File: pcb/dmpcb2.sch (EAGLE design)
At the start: 65 parts, among them IC1 7805DT, IC2 L293D, IC4 LM358D, IC5 LM358D, J7 SJ-3523-SMT-TR, Q1 IRF530, Q2 IRF530

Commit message: borading2..
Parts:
- added DCMOTOR1: (no value), SparkFun-Connectors:CONN_022.54MM_SCREWTERM
- added JP1: (no value), jumper:JP2E
- added X2: (no value), con-wago-500:W237-4
- added X3: (no value), con-wago-500:W237-102
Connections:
- new net N$11: DCMOTOR1.1, IC2.4Y
- new net N$12: DCMOTOR1.2, IC2.3Y
- net +5V: now also JP1.3
- net A1: now also X2-2.KL
- net A2: now also X2-1.KL
- net B1: now also X2-3.KL
- net B2: now also X2-4.KL
- net GND: now also X3-2.KL
- net V+: now also JP1.1
- net VMOT: now also JP1.2, X3-1.KL
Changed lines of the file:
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@@
 <part name="D3" library="diode" library_urn="urn:adsk.eagle:library:210" deviceset="1N4148" device="DO35-7" package3d_urn="urn:adsk.eagle:package:43339/2"/>
 <part name="D4" library="diode" library_urn="urn:adsk.eagle:library:210" deviceset="1N4148" device="DO35-7" package3d_urn="urn:adsk.eagle:package:43339/2"/>
+<part name="X2" library="con-wago-500" library_urn="urn:adsk.eagle:library:195" deviceset="W237-4" device="" package3d_urn="urn:adsk.eagle:package:10695/1"/>
+<part name="X3" library="con-wago-500" library_urn="urn:adsk.eagle:library:195" deviceset="W237-102" device="" package3d_urn="urn:adsk.eagle:package:10688/1"/>
+<part name="GND25" library="supply1" library_urn="urn:adsk.eagle:library:371" deviceset="GND" device=""/>
+<part name="JP1" library="jumper" library_urn="urn:adsk.eagle:library:252" deviceset="JP2E" device="" package3d_urn="urn:adsk.eagle:package:15452/1"/>
+<part name="SUPPLY16" library="supply2" library_urn="urn:adsk.eagle:library:372" deviceset="+5V" device=""/>
+<part name="DCMOTOR1" library="SparkFun-Connectors" library_urn="urn:adsk.eagle:library:513" deviceset="CONN_02" device="2.54MM_SCREWTERM" package3d_urn="urn:adsk.eagle:package:38059/1"/>
 </parts>
 <sheets>
@@
 <attribute name="VALUE" x="261.62" y="116.6114" size="1.778" layer="96" rot="R180"/>
 </instance>
+<instance part="X2" gate="-1" x="414.02" y="91.44" smashed="yes" rot="R180">
+<attribute name="NAME" x="414.02" y="90.551" size="1.778" layer="95"/>
+</instance>
+<instance part="X2" gate="-2" x="414.02" y="96.52" smashed="yes" rot="R180">
+<attribute name="NAME" x="414.02" y="95.631" size="1.778" layer="95"/>
+</instance>
+<instance part="X2" gate="-3" x="414.02" y="101.6" smashed="yes" rot="R180">
+<attribute name="NAME" x="414.02" y="100.711" size="1.778" layer="95"/>
+</instance>
+<instance part="X2" gate="-4" x="414.02" y="106.68" smashed="yes" rot="R180">
+<attribute name="VALUE" x="416.56" y="110.363" size="1.778" layer="96" rot="R180"/>
+<attribute name="NAME" x="414.02" y="105.791" size="1.778" layer="95"/>
+</instance>
+<instance part="X3" gate="-1" x="414.02" y="114.3" smashed="yes" rot="R180">
+<attribute name="NAME" x="414.02" y="113.411" size="1.778" layer="95"/>
+</instance>
+<instance part="X3" gate="-2" x="414.02" y="121.92" smashed="yes" rot="R180">
+<attribute name="VALUE" x="416.56" y="125.603" size="1.778" layer="96" rot="R180"/>
+<attribute name="NAME" x="414.02" y="121.031" size="1.778" layer="95"/>
+</instance>
+<instance part="GND25" gate="1" x="393.7" y="121.92" smashed="yes" rot="R270">
+<attribute name="VALUE" x="391.16" y="124.46" size="1.778" layer="96" rot="R270"/>
+</instance>
+<instance part="JP1" gate="1" x="406.4" y="137.16" smashed="yes">
+<attribute name="NAME" x="402.59" y="137.16" size="1.778" layer="95" rot="R90"/>
+<attribute name="VALUE" x="412.115" y="137.16" size="1.778" layer="96" rot="R90"/>
+</instance>
+<instance part="SUPPLY16" gate="+5V" x="416.56" y="132.08" smashed="yes" rot="R270">
+<attribute name="VALUE" x="419.735" y="132.715" size="1.778" layer="96"/>
+</instance>
+<instance part="DCMOTOR1" gate="G$1" x="411.48" y="187.96" smashed="yes" rot="R180">
+<attribute name="VALUE" x="414.02" y="192.786" size="1.778" layer="96" font="vector" rot="R180"/>
+<attribute name="NAME" x="414.02" y="182.372" size="1.778" layer="95" font="vector" rot="R180"/>
+</instance>
 </instances>
 <busses>
@@
 <junction x="297.18" y="114.3"/>
 </segment>
+<segment>
+<pinref part="X3" gate="-2" pin="KL"/>
+<wire x1="408.94" y1="121.92" x2="396.24" y2="121.92" width="0.1524" layer="91"/>
+<pinref part="GND25" gate="1" pin="GND"/>
+</segment>
 </net>
 <net name="V+" class="0">
@@
 <wire x1="345.44" y1="154.94" x2="345.44" y2="162.56" width="0.1524" layer="91"/>
 <wire x1="345.44" y1="162.56" x2="347.98" y2="162.56" width="0.1524" layer="91"/>
+</segment>
+<segment>
+<pinref part="JP1" gate="1" pin="1"/>
+<wire x1="403.86" y1="134.62" x2="403.86" y2="127" width="0.1524" layer="91"/>
+<wire x1="403.86" y1="127" x2="414.02" y2="127" width="0.1524" layer="91"/>
+<label x="414.02" y="127" size="1.778" layer="95"/>
 </segment>
 </net>
@@
 <wire x1="114.3" y1="129.54" x2="114.3" y2="121.92" width="0.1524" layer="91"/>
 </segment>
+<segment>
+<pinref part="JP1" gate="1" pin="3"/>
+<wire x1="408.94" y1="134.62" x2="408.94" y2="132.08" width="0.1524" layer="91"/>
+<wire x1="408.94" y1="132.08" x2="414.02" y2="132.08" width="0.1524" layer="91"/>
+<pinref part="SUPPLY16" gate="+5V" pin="+5V"/>
+</segment>
 </net>
 <net name="N$2" class="0">
@@
 <net name="B2" class="0">
 <segment>
-<wire x1="373.38" y1="101.6" x2="375.92" y2="101.6" width="0.1524" layer="91"/>
 <label x="375.92" y="101.6" size="1.778" layer="95" xref="yes"/>
 <pinref part="U$2" gate="G$1" pin="B2"/>
+<pinref part="X2" gate="-4" pin="KL"/>
+<wire x1="408.94" y1="106.68" x2="396.24" y2="106.68" width="0.1524" layer="91"/>
+<wire x1="396.24" y1="106.68" x2="396.24" y2="101.6" width="0.1524" layer="91"/>
+<wire x1="396.24" y1="101.6" x2="373.38" y2="101.6" width="0.1524" layer="91"/>
 </segment>
 </net>
@@
 <segment>
 <label x="386.08" y="99.06" size="1.778" layer="95" xref="yes"/>
-<wire x1="373.38" y1="99.06" x2="386.08" y2="99.06" width="0.1524" layer="91"/>
 <pinref part="U$2" gate="G$1" pin="B1"/>
+<wire x1="373.38" y1="99.06" x2="403.86" y2="99.06" width="0.1524" layer="91"/>
+<wire x1="403.86" y1="99.06" x2="403.86" y2="101.6" width="0.1524" layer="91"/>
+<pinref part="X2" gate="-3" pin="KL"/>
+<wire x1="403.86" y1="101.6" x2="408.94" y2="101.6" width="0.1524" layer="91"/>
 </segment>
 </net>
 <net name="A1" class="0">
 <segment>
-<wire x1="373.38" y1="96.52" x2="375.92" y2="96.52" width="0.1524" layer="91"/>
 <label x="375.92" y="96.52" size="1.778" layer="95" xref="yes"/>
 <pinref part="U$2" gate="G$1" pin="A1"/>
+<pinref part="X2" gate="-2" pin="KL"/>
+<wire x1="373.38" y1="96.52" x2="408.94" y2="96.52" width="0.1524" layer="91"/>
 </segment>
 </net>
@@
 <segment>
 <label x="386.08" y="93.98" size="1.778" layer="95" xref="yes"/>
-<wire x1="373.38" y1="93.98" x2="386.08" y2="93.98" width="0.1524" layer="91"/>
+<wire x1="373.38" y1="93.98" x2="393.7" y2="93.98" width="0.1524" layer="91"/>
 <pinref part="U$2" gate="G$1" pin="A2"/>
+<wire x1="393.7" y1="93.98" x2="393.7" y2="91.44" width="0.1524" layer="91"/>
+<pinref part="X2" gate="-1" pin="KL"/>
+<wire x1="393.7" y1="91.44" x2="408.94" y2="91.44" width="0.1524" layer="91"/>
 </segment>
 </net>
@@
 <wire x1="373.38" y1="114.3" x2="381" y2="114.3" width="0.1524" layer="91"/>
 <pinref part="C7" gate="G$1" pin="+"/>
-<wire x1="381" y1="114.3" x2="386.08" y2="114.3" width="0.1524" layer="91"/>
 <label x="386.08" y="114.3" size="1.778" layer="95" xref="yes"/>
+<wire x1="381" y1="114.3" x2="406.4" y2="114.3" width="0.1524" layer="91"/>
+<pinref part="X3" gate="-1" pin="KL"/>
+<wire x1="406.4" y1="114.3" x2="408.94" y2="114.3" width="0.1524" layer="91"/>
+<wire x1="406.4" y1="114.3" x2="406.4" y2="134.62" width="0.1524" layer="91"/>
+<junction x="406.4" y="114.3"/>
+<pinref part="JP1" gate="1" pin="2"/>
 </segment>
 </net>
@@
 </segment>
 </net>
+<net name="N$11" class="0">
+<segment>
+<pinref part="IC2" gate="G$1" pin="4Y"/>
+<pinref part="DCMOTOR1" gate="G$1" pin="1"/>
+<wire x1="378.46" y1="187.96" x2="403.86" y2="187.96" width="0.1524" layer="91"/>
+</segment>
+</net>
+<net name="N$12" class="0">
+<segment>
+<pinref part="DCMOTOR1" gate="G$1" pin="2"/>
+<wire x1="403.86" y1="185.42" x2="391.16" y2="185.42" width="0.1524" layer="91"/>
+<wire x1="391.16" y1="185.42" x2="391.16" y2="172.72" width="0.1524" layer="91"/>
+<pinref part="IC2" gate="G$1" pin="3Y"/>
+<wire x1="391.16" y1="172.72" x2="378.46" y2="172.72" width="0.1524" layer="91"/>
+</segment>
+</net>

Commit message: routing done
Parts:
- removed DCMOTOR, DCMOTOR1, SENSOR, SWITCHLOAD, SWITCHLOAD1: (no value), SparkFun-Connectors:CONN_022.54MM_SCREWTERM
- removed SV2: (no value), con-lstb:MA08-1
- added J3: (no value), SparkFun-Connectors:CONN_08"
- added J4: (no value), SparkFun-Connectors:CONN_03LOCK_LONGPADS
- added X4, X5, X6, X7, X8: (no value), con-wago-500:W237-102
- renumbered JP7 to EXT_5V, JP8 to 14/DAC
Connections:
- removed net LM293EN: IC2.1-2EN, SV2.3
- removed net LM293IN01: IC2.1A, SV2.4
- removed net LM293IN02: IC2.2A, SV2.5
- new net H-BRDIGE_A_02: IC2.2A, J3.5
- new net H-BRIDGE_A_01: IC2.1A, J3.4
- new net H-BRIDGE_A_EN: IC2.1-2EN, J3.3
- new net H-BRIDGE_B_01: IC2.4A, J4.3
- new net H-BRIDGE_B_02: IC2.3A, J4.2
- new net H-BRIDGE_B_EN: IC2.3-4EN, J4.1
- net +5V: now also X8-1.KL; no longer SENSOR.2
- net BUTTON01: now also J3.1; no longer SV2.1
- net BUTTON02: now also J3.2; no longer SV2.2
- net DRV8825DIR: now also J1.1; no longer J1.2
- net DRV8825EN: now also J1.5; no longer J1.1
- net DRV8825SLP: now also J1.3; no longer J1.5
- net DRV8825STEP: now also J1.2; no longer J1.3
- net M1: now also X4-2.KL; no longer SWITCHLOAD.1
- net M2: now also X5-2.KL; no longer SWITCHLOAD1.1
- net MAX7219CLK: now also J3.7; no longer SV2.7
- net MAX7219CS: now also J3.8; no longer SV2.8
- net MAX7219DIN: now also J3.6; no longer SV2.6
- net N$11: now also X6-2.KL; no longer DCMOTOR1.1
- net N$12: now also X6-1.KL; no longer DCMOTOR1.2
- net N$5: now also X7-1.KL; no longer DCMOTOR.2
- net N$6: now also X7-2.KL; no longer DCMOTOR.1
- net SENSORPORT: now also X8-2.KL; no longer SENSOR.1
- net V+: now also X4-1.KL, X5-1.KL; no longer SWITCHLOAD.2, SWITCHLOAD1.2
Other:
- moved on the sheet: JP3

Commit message: started to add part references and values, also started adding pin names and similar. tried adding nice graphics as bmp but failed horribly...
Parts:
- R4: value 220 -> 220R
- renumbered JP6 to STP_CONF, LED1 to LED_01, U$1 to TEENSY3.2, U$2 to DRV8825

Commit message: issues added and fixed
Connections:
- removed net N$19: S1.S, S1.S1
- removed net N$21: S2.S, S2.S1
- net 3.3V: now also S1.S, S1.S1, S2.S, S2.S1
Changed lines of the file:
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@@
 <?xml version="1.0" encoding="utf-8"?>
 <!DOCTYPE eagle SYSTEM "eagle.dtd">
-<eagle version="9.4.2">
+<eagle version="9.5.2">
 <drawing>
 <settings>
@@
 <wire x1="187.96" y1="157.48" x2="187.96" y2="152.4" width="0.1524" layer="91"/>
 <label x="187.96" y="152.4" size="1.778" layer="95" rot="R270" xref="yes"/>
-<label x="261.62" y="43.18" size="1.778" layer="95" rot="R90" xref="yes"/>
-</segment>
-<segment>
-<label x="289.56" y="43.18" size="1.778" layer="95" rot="R90" xref="yes"/>
 </segment>
 <segment>
@@
 <wire x1="83.82" y1="124.46" x2="83.82" y2="116.84" width="0.1524" layer="91"/>
 </segment>
+<segment>
+<pinref part="S1" gate="1" pin="S"/>
+<wire x1="261.62" y1="43.18" x2="261.62" y2="40.64" width="0.1524" layer="91"/>
+<pinref part="S1" gate="1" pin="S1"/>
+<wire x1="261.62" y1="40.64" x2="264.16" y2="40.64" width="0.1524" layer="91"/>
+<junction x="264.16" y="40.64"/>
+<junction x="261.62" y="40.64"/>
+<pinref part="S2" gate="1" pin="S"/>
+<wire x1="289.56" y1="43.18" x2="289.56" y2="40.64" width="0.1524" layer="91"/>
+<pinref part="S2" gate="1" pin="S1"/>
+<wire x1="289.56" y1="40.64" x2="292.1" y2="40.64" width="0.1524" layer="91"/>
+<junction x="289.56" y="40.64"/>
+<junction x="292.1" y="40.64"/>
+<wire x1="261.62" y1="43.18" x2="289.56" y2="43.18" width="0.1524" layer="91"/>
+<label x="274.32" y="43.18" size="1.778" layer="95" rot="R90" xref="yes"/>
+</segment>
 </net>
 <net name="N$14" class="0">
@@
 </segment>
 </net>
-<net name="N$19" class="0">
-<segment>
-<pinref part="S1" gate="1" pin="S"/>
-<wire x1="261.62" y1="43.18" x2="261.62" y2="40.64" width="0.1524" layer="91"/>
-<pinref part="S1" gate="1" pin="S1"/>
-<wire x1="261.62" y1="40.64" x2="264.16" y2="40.64" width="0.1524" layer="91"/>
-<junction x="264.16" y="40.64"/>
-<junction x="261.62" y="40.64"/>
-</segment>
-</net>
-<net name="N$21" class="0">
-<segment>
-<pinref part="S2" gate="1" pin="S"/>
-<wire x1="289.56" y1="43.18" x2="289.56" y2="40.64" width="0.1524" layer="91"/>
-<pinref part="S2" gate="1" pin="S1"/>
-<wire x1="289.56" y1="40.64" x2="292.1" y2="40.64" width="0.1524" layer="91"/>
-<junction x="289.56" y="40.64"/>
-<junction x="292.1" y="40.64"/>
-</segment>
-</net>

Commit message: added possibilty to jump out the lm7805
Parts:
- added EXT_5V1: (no value), jumper:JP1E
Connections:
- new net N$19: EXT_5V1.2, IC1.VI
- net +5V: now also LED_01.A
- net N$25: no longer LED_01.A
- net V+: now also EXT_5V1.1; no longer IC1.VI
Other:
- moved on the sheet: LED_01, R4
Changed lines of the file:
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@@
 <part name="J3" library="SparkFun-Connectors" deviceset="CONN_08" device="&quot;"/>
 <part name="J4" library="SparkFun-Connectors" library_urn="urn:adsk.eagle:library:513" deviceset="CONN_03" device="LOCK_LONGPADS" package3d_urn="urn:adsk.eagle:package:38065/1"/>
+<part name="EXT_5V1" library="jumper" library_urn="urn:adsk.eagle:library:252" deviceset="JP1E" device="" package3d_urn="urn:adsk.eagle:package:15455/1"/>
 </parts>
 <sheets>
@@
 <attribute name="VALUE" x="54.102" y="196.85" size="1.778" layer="96" rot="R90"/>
 </instance>
-<instance part="LED_01" gate="G$1" x="104.14" y="175.26" smashed="yes">
-<attribute name="NAME" x="107.696" y="170.688" size="1.778" layer="95" rot="R90"/>
-<attribute name="VALUE" x="109.855" y="170.688" size="1.778" layer="96" rot="R90"/>
-</instance>
-<instance part="R4" gate="G$1" x="104.14" y="162.56" smashed="yes" rot="R90">
-<attribute name="NAME" x="102.6414" y="158.75" size="1.778" layer="95" rot="R90"/>
-<attribute name="VALUE" x="107.442" y="158.75" size="1.778" layer="96" rot="R90"/>
-</instance>
-<instance part="GND9" gate="1" x="104.14" y="152.4" smashed="yes">
-<attribute name="VALUE" x="101.6" y="149.86" size="1.778" layer="96"/>
+<instance part="LED_01" gate="G$1" x="119.38" y="175.26" smashed="yes">
+<attribute name="NAME" x="122.936" y="170.688" size="1.778" layer="95" rot="R90"/>
+<attribute name="VALUE" x="125.095" y="170.688" size="1.778" layer="96" rot="R90"/>
+</instance>
+<instance part="R4" gate="G$1" x="119.38" y="165.1" smashed="yes" rot="R90">
+<attribute name="NAME" x="117.8814" y="161.29" size="1.778" layer="95" rot="R90"/>
+<attribute name="VALUE" x="122.682" y="161.29" size="1.778" layer="96" rot="R90"/>
+</instance>
+<instance part="GND9" gate="1" x="119.38" y="154.94" smashed="yes">
+<attribute name="VALUE" x="116.84" y="152.4" size="1.778" layer="96"/>
 </instance>
 <instance part="Q1" gate="G$1" x="287.02" y="111.76" smashed="yes" rot="R90">
@@
 <attribute name="VALUE" x="434.34" y="177.546" size="1.778" layer="96" font="vector" rot="R180"/>
 <attribute name="NAME" x="434.34" y="164.592" size="1.778" layer="95" font="vector" rot="R180"/>
+</instance>
+<instance part="EXT_5V1" gate="A" x="58.42" y="195.58" smashed="yes">
+<attribute name="NAME" x="57.15" y="195.58" size="1.778" layer="95" rot="R90"/>
+<attribute name="VALUE" x="64.135" y="195.58" size="1.778" layer="96" rot="R90"/>
 </instance>
 </instances>
@@
 <pinref part="R4" gate="G$1" pin="1"/>
 <pinref part="GND9" gate="1" pin="GND"/>
-<wire x1="104.14" y1="157.48" x2="104.14" y2="154.94" width="0.1524" layer="91"/>
+<wire x1="119.38" y1="160.02" x2="119.38" y2="157.48" width="0.1524" layer="91"/>
 </segment>
 <segment>
@@
 <wire x1="40.64" y1="193.04" x2="40.64" y2="182.88" width="0.1524" layer="91"/>
 <label x="48.26" y="185.42" size="1.778" layer="95"/>
-<pinref part="IC1" gate="A1" pin="VI"/>
 <wire x1="40.64" y1="182.88" x2="50.8" y2="182.88" width="0.1524" layer="91"/>
 <pinref part="C1" gate="G$1" pin="+"/>
 <wire x1="50.8" y1="182.88" x2="55.88" y2="182.88" width="0.1524" layer="91"/>
-<wire x1="55.88" y1="182.88" x2="63.5" y2="182.88" width="0.1524" layer="91"/>
 <wire x1="55.88" y1="182.88" x2="55.88" y2="177.8" width="0.1524" layer="91"/>
-<junction x="55.88" y="182.88"/>
 <pinref part="C3" gate="G$1" pin="+"/>
 <wire x1="50.8" y1="187.96" x2="50.8" y2="182.88" width="0.1524" layer="91"/>
@@
 <pinref part="X1" gate="-1" pin="KL"/>
 <junction x="40.64" y="182.88"/>
+<pinref part="EXT_5V1" gate="A" pin="1"/>
+<wire x1="55.88" y1="182.88" x2="58.42" y2="182.88" width="0.1524" layer="91"/>
+<wire x1="58.42" y1="182.88" x2="58.42" y2="193.04" width="0.1524" layer="91"/>
+<junction x="55.88" y="182.88"/>
 </segment>
 <segment>
@@
 <wire x1="114.3" y1="193.04" x2="114.3" y2="182.88" width="0.1524" layer="91"/>
 <pinref part="SUPPLY2" gate="+5V" pin="+5V"/>
-<wire x1="114.3" y1="182.88" x2="124.46" y2="182.88" width="0.1524" layer="91"/>
+<wire x1="114.3" y1="182.88" x2="119.38" y2="182.88" width="0.1524" layer="91"/>
+<pinref part="LED_01" gate="G$1" pin="A"/>
+<wire x1="119.38" y1="182.88" x2="124.46" y2="182.88" width="0.1524" layer="91"/>
+<wire x1="119.38" y1="177.8" x2="119.38" y2="182.88" width="0.1524" layer="91"/>
+<junction x="119.38" y="182.88"/>
 </segment>
 <segment>
@@
 <pinref part="LED_01" gate="G$1" pin="C"/>
 <pinref part="R4" gate="G$1" pin="2"/>
-<wire x1="104.14" y1="170.18" x2="104.14" y2="167.64" width="0.1524" layer="91"/>
 </segment>
 </net>
@@
 <pinref part="C2" gate="G$1" pin="+"/>
 <wire x1="83.82" y1="182.88" x2="88.9" y2="182.88" width="0.1524" layer="91"/>
-<wire x1="88.9" y1="182.88" x2="104.14" y2="182.88" width="0.1524" layer="91"/>
+<wire x1="88.9" y1="182.88" x2="111.76" y2="182.88" width="0.1524" layer="91"/>
 <wire x1="88.9" y1="182.88" x2="88.9" y2="177.8" width="0.1524" layer="91"/>
 <junction x="88.9" y="182.88"/>
-<pinref part="LED_01" gate="G$1" pin="A"/>
-<wire x1="104.14" y1="177.8" x2="104.14" y2="182.88" width="0.1524" layer="91"/>
 <pinref part="EXT_5V" gate="A" pin="1"/>
 <wire x1="111.76" y1="193.04" x2="111.76" y2="182.88" width="0.1524" layer="91"/>
-<wire x1="111.76" y1="182.88" x2="104.14" y2="182.88" width="0.1524" layer="91"/>
-<junction x="104.14" y="182.88"/>
 </segment>
 </net>
@@
 </segment>
 </net>
+<net name="N$19" class="0">
+<segment>
+<pinref part="EXT_5V1" gate="A" pin="2"/>
+<wire x1="60.96" y1="193.04" x2="60.96" y2="182.88" width="0.1524" layer="91"/>
+<pinref part="IC1" gate="A1" pin="VI"/>
+<wire x1="60.96" y1="182.88" x2="63.5" y2="182.88" width="0.1524" layer="91"/>
+</segment>
+</net>

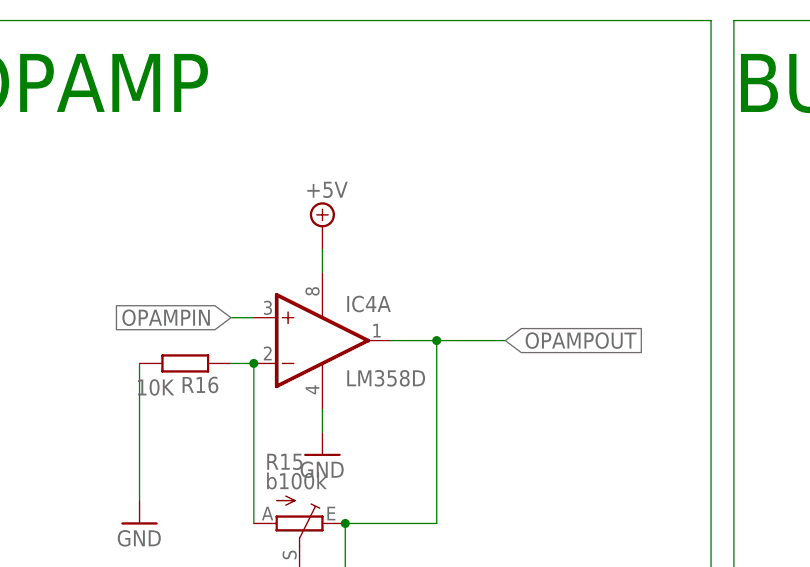
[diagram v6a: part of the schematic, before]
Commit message: moved bypass caps
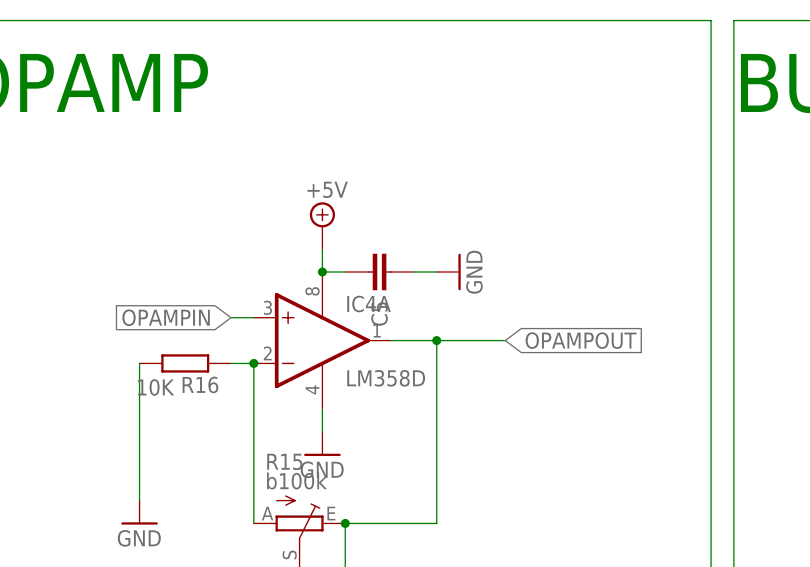
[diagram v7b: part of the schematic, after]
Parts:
- added C5: 100nf, rcl:C-EUC0805
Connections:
- net +5V: now also C5.1
- net GND: now also C5.2
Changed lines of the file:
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@@
 <part name="J4" library="SparkFun-Connectors" library_urn="urn:adsk.eagle:library:513" deviceset="CONN_03" device="LOCK_LONGPADS" package3d_urn="urn:adsk.eagle:package:38065/1"/>
 <part name="EXT_5V1" library="jumper" library_urn="urn:adsk.eagle:library:252" deviceset="JP1E" device="" package3d_urn="urn:adsk.eagle:package:15455/1"/>
+<part name="C5" library="rcl" library_urn="urn:adsk.eagle:library:334" deviceset="C-EU" device="C0805" package3d_urn="urn:adsk.eagle:package:23617/2" value="100nf"/>
+<part name="GND27" library="supply1" library_urn="urn:adsk.eagle:library:371" deviceset="GND" device=""/>
 </parts>
 <sheets>
@@
 <attribute name="VALUE" x="64.135" y="195.58" size="1.778" layer="96" rot="R90"/>
 </instance>
+<instance part="C5" gate="G$1" x="198.12" y="38.1" smashed="yes" rot="R90">
+<attribute name="NAME" x="200.279" y="32.004" size="1.778" layer="95" rot="R90"/>
+</instance>
+<instance part="GND27" gate="1" x="208.28" y="38.1" smashed="yes" rot="R90">
+<attribute name="VALUE" x="210.82" y="35.56" size="1.778" layer="96" rot="R90"/>
+</instance>
 </instances>
 <busses>
@@
 <pinref part="GND25" gate="1" pin="GND"/>
 </segment>
+<segment>
+<pinref part="C5" gate="G$1" pin="2"/>
+<pinref part="GND27" gate="1" pin="GND"/>
+<wire x1="203.2" y1="38.1" x2="205.74" y2="38.1" width="0.1524" layer="91"/>
+</segment>
 </net>
 <net name="V+" class="0">
@@
 <pinref part="IC4" gate="P" pin="V+"/>
 <wire x1="193.04" y1="40.64" x2="193.04" y2="38.1" width="0.1524" layer="91"/>
-</segment>
-<segment>
+<pinref part="C5" gate="G$1" pin="1"/>
+<wire x1="193.04" y1="38.1" x2="195.58" y2="38.1" width="0.1524" layer="91"/>
+<junction x="193.04" y="38.1"/>
+</segment>
+<segment>
